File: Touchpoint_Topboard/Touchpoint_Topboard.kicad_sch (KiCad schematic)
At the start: 0 parts

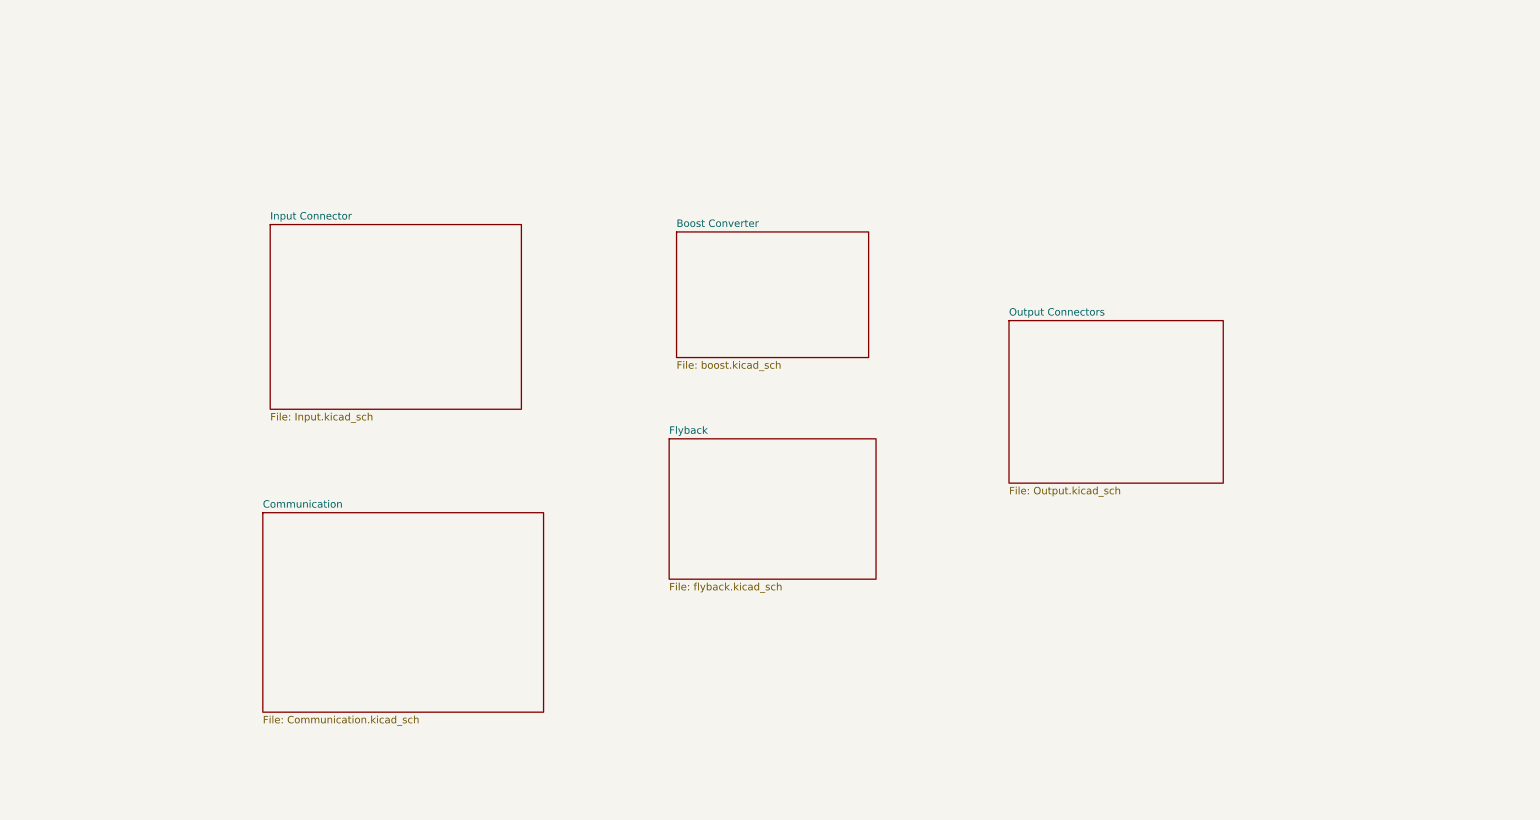
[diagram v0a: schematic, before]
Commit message: Added remaining interface things to topboard schematic
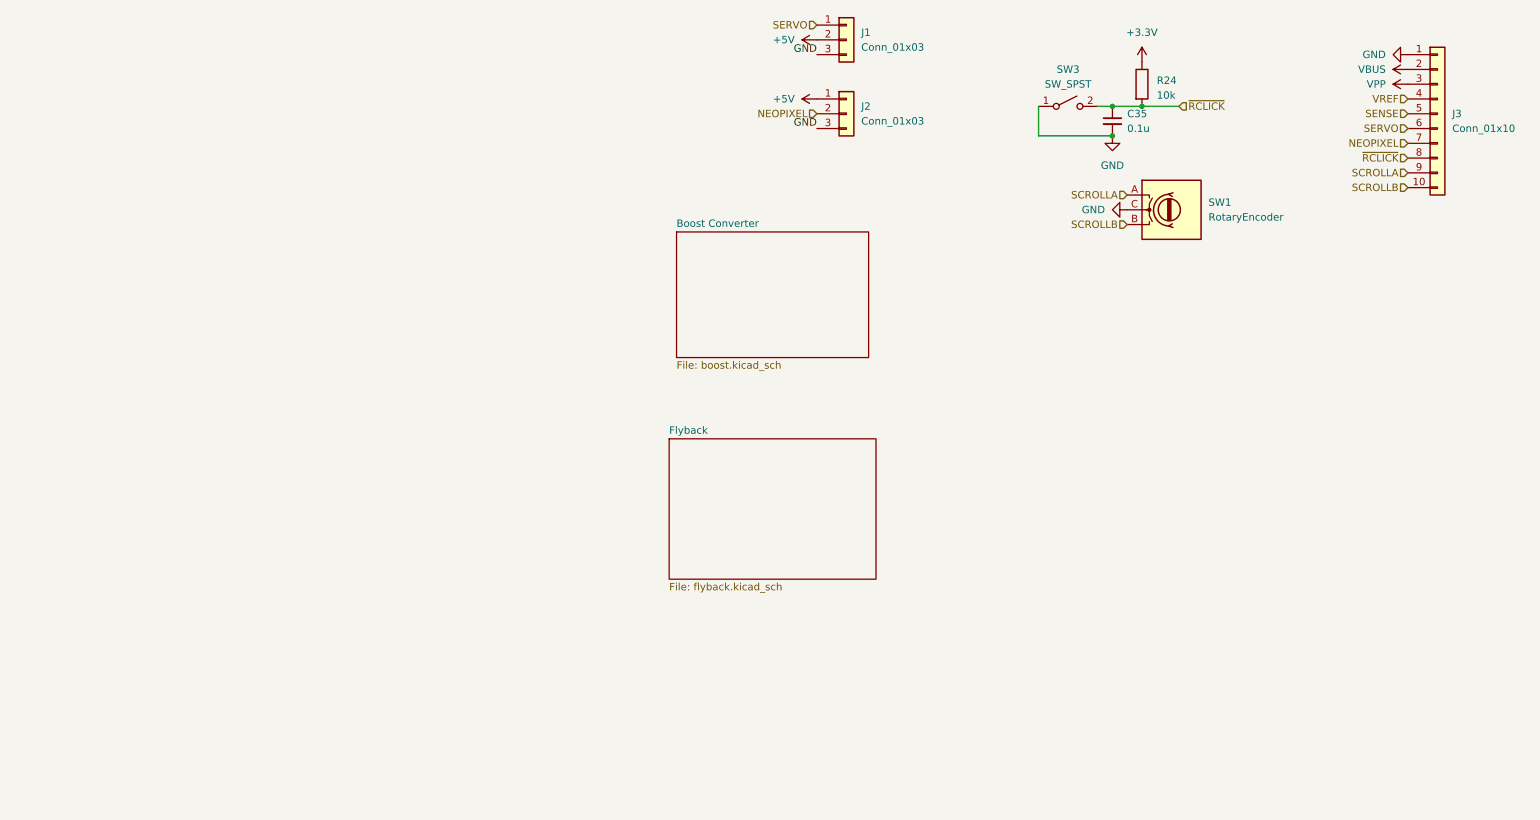
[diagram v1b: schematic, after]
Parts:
- added C35: 0.1u, Capacitor_SMD:C_0402_1005Metric, symbol Device:C_Small
- added J1, J2: Conn_01x03, symbol Connector_Generic:Conn_01x03
- added J3: Conn_01x10, symbol Connector_Generic:Conn_01x10
- added R24: 10k, Resistor_SMD:R_0402_1005Metric, symbol Device:R
- added SW1: RotaryEncoder, symbol Device:RotaryEncoder
- added SW3: SW_SPST, Button_Switch_THT:SW_PUSH_6mm, symbol Switch:SW_SPST
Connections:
- new net +3.3V: R24.1
- new net +5V: J1.2 (Pin_2), J2.1 (Pin_1)
- new net GND: C35.2, J1.3 (Pin_3), J2.3 (Pin_3), J3.1 (Pin_1), SW1.C, SW3.1 (A)
- new net NEOPIXEL: J2.2 (Pin_2), J3.7 (Pin_7)
- new net SCROLLA: J3.9 (Pin_9), SW1.A
- new net SCROLLB: J3.10 (Pin_10), SW1.B
- new net SENSE: J3.5 (Pin_5)
- new net SERVO: J1.1 (Pin_1), J3.6 (Pin_6)
- new net VBUS: J3.2 (Pin_2)
- new net VPP: J3.3 (Pin_3)
- new net VREF: J3.4 (Pin_4)
- new net ~{RCLICK}: C35.1, J3.8 (Pin_8), R24.2, SW3.2 (B)
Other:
- removed sheet Communication
- removed sheet Input Connector
- removed sheet Output Connectors

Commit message: Finished assigning most footprints
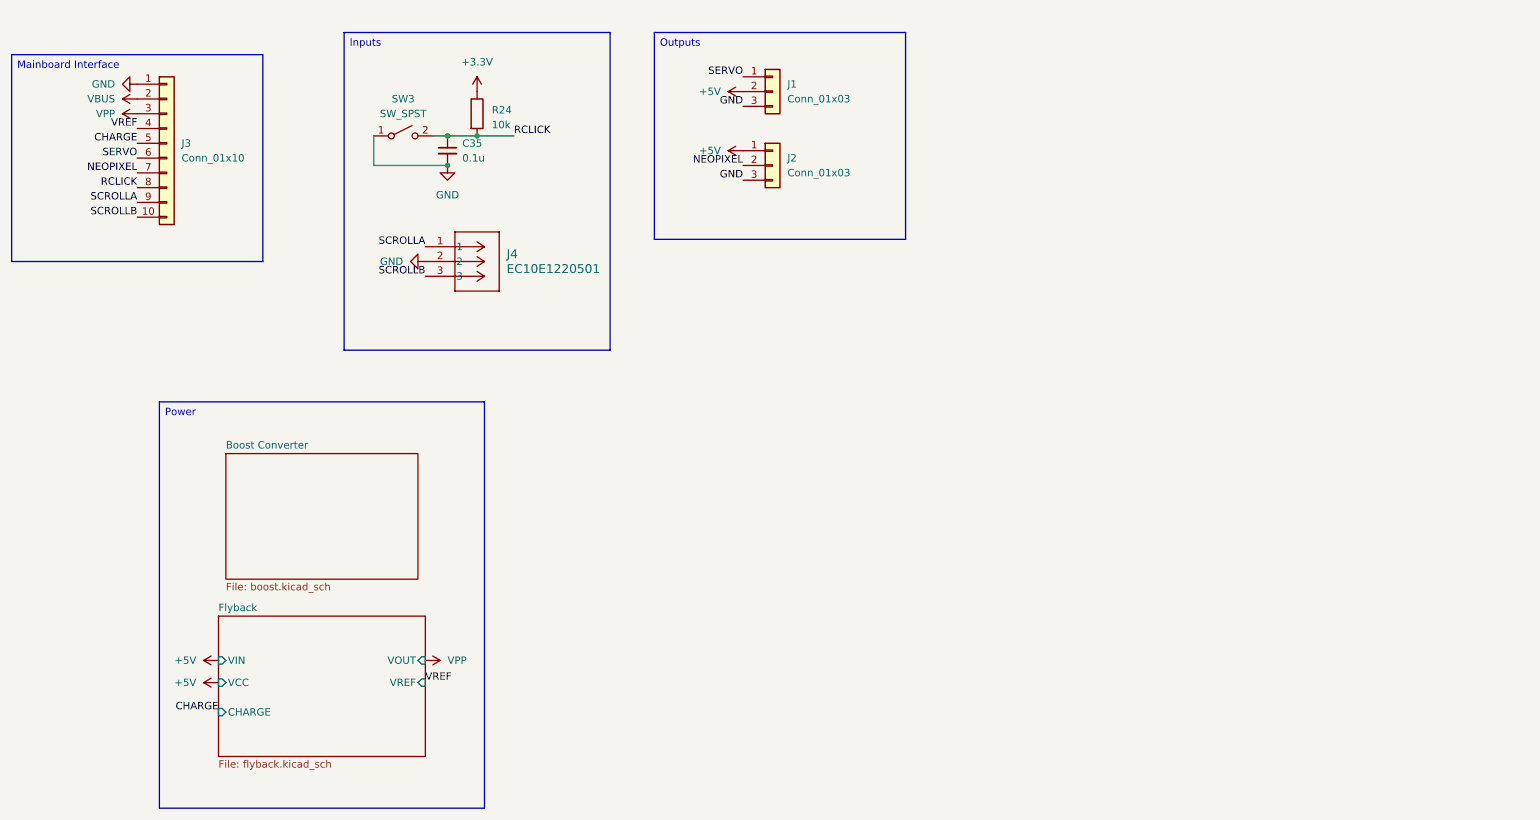
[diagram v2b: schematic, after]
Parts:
- removed SW1: RotaryEncoder, symbol Device:RotaryEncoder
- added J4: EC10E1220501, Touchpoint:CONN03_EC10E_9P8X6P1_ALPS, symbol EC10E122:EC10E1220501
- J1, J2: footprint (none) -> Connector_PinHeader_2.54mm:PinHeader_1x03_P2.54mm_Vertical
- J3: footprint (none) -> Connector_PinSocket_2.54mm:PinSocket_1x10_P2.54mm_Vertical
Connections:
- net GND: now also J4.2
- net SCROLLA: now also J4.1
- net SCROLLB: now also J4.3
- net SENSE renamed CHARGE
- net ~{RCLICK} renamed RCLICK
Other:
- sheet Flyback ports: added CHARGE, VCC, VIN, VOUT, VREF; removed none
- moved on the sheet: C35, J1, J2, J3, R24, SW3

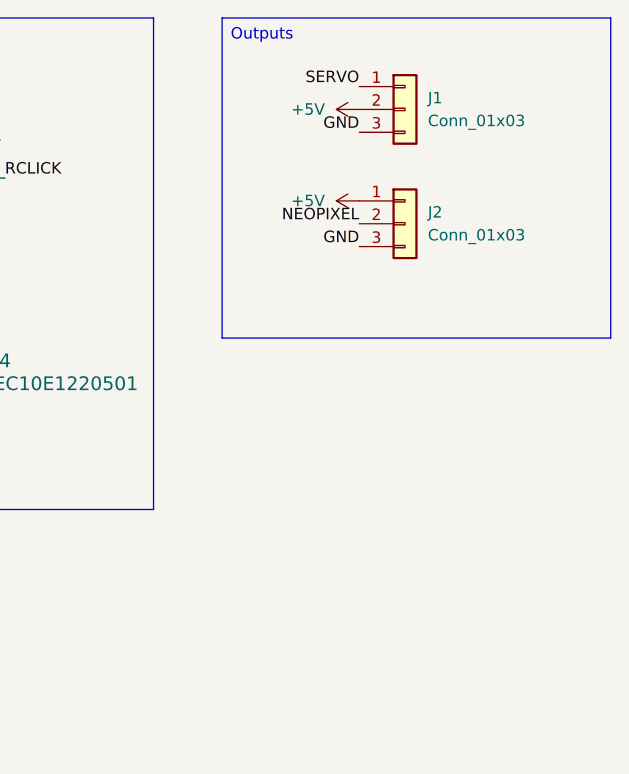
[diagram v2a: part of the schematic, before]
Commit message: Changed some component values based on availability
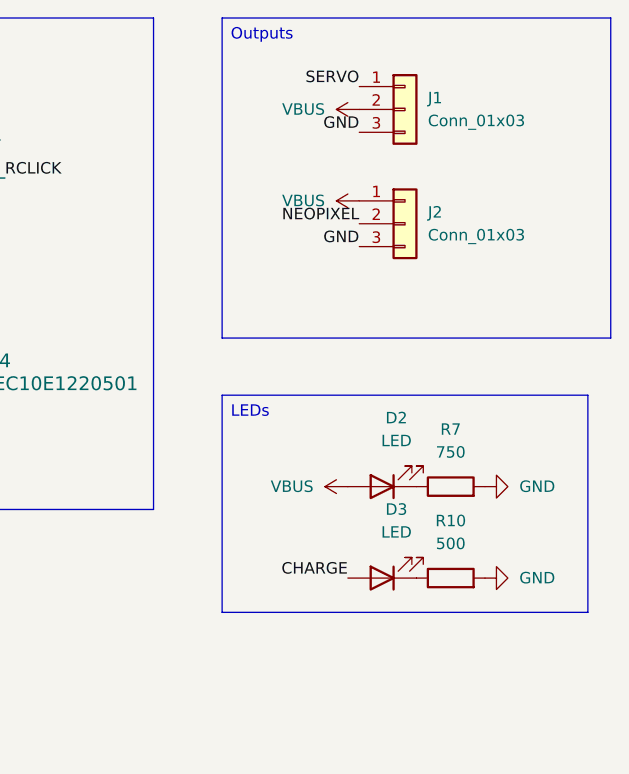
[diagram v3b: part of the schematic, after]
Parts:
- added D2, D3: LED, LED_SMD:LED_0603_1608Metric, symbol Device:LED
- added R10: 500, Resistor_SMD:R_0402_1005Metric, symbol Device:R
- added R7: 750, Resistor_SMD:R_0402_1005Metric, symbol Device:R
- SW3: footprint Button_Switch_THT:SW_PUSH_6mm -> (none)
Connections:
- net +5V: no longer J1.2 (Pin_2), J2.1 (Pin_1)
- net CHARGE: now also D3.2 (A)
- net GND: now also R10.2, R7.2
- net VBUS: now also J1.2 (Pin_2), J2.1 (Pin_1), D2.2 (A)
- new net: D2.1 (K), R7.1
- new net: D3.1 (K), R10.1

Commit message: Finished assigning footprints and 3d models for both boards
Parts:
- SW3: footprint (none) -> Touchpoint:SW_SPST_EVQP0
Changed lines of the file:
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@@
 			)
 		)
-		(property "Footprint" ""
+		(property "Footprint" "Touchpoint:SW_SPST_EVQP0"
 			(at 86.36 36.83 0)
 			(effects

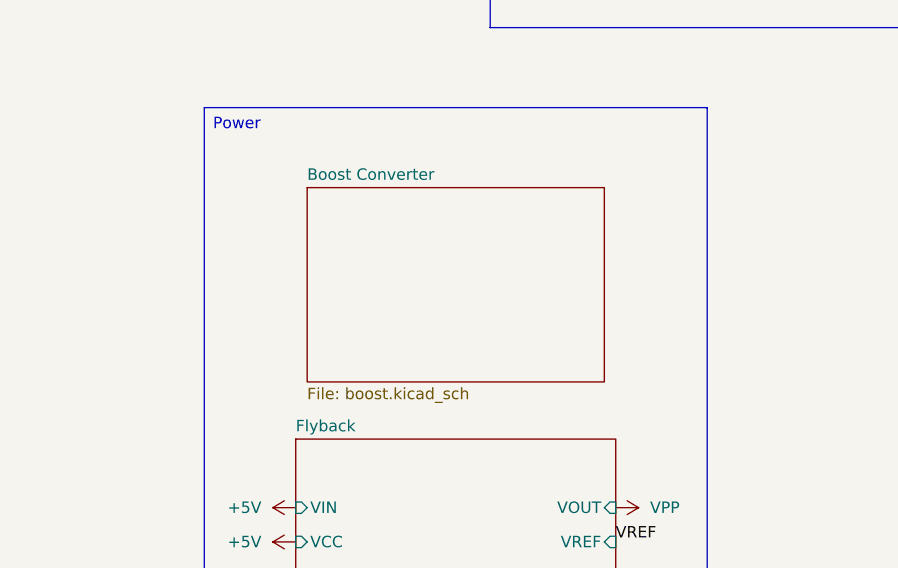
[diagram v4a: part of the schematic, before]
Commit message: Added 5V regulator to flyback converter
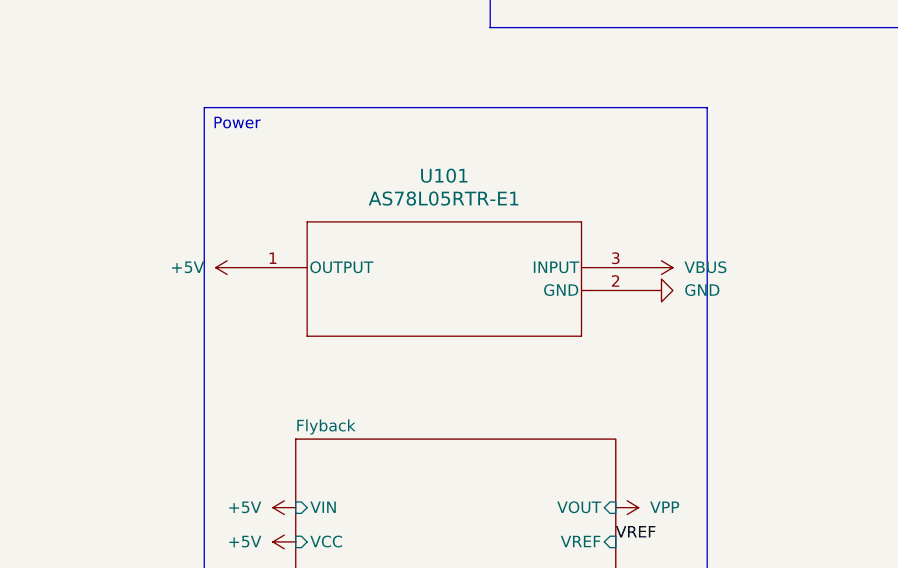
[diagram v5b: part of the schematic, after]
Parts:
- added U101: AS78L05RTR-E1, Touchpoint:SOT-89_3MC_MCH, symbol AS78LO5RTR:AS78L05RTR-E1
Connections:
- net +5V: now also U101.1 (OUTPUT)
- net GND: now also U101.2 (GND)
- net VBUS: now also U101.3 (INPUT)
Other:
- removed sheet Boost Converter

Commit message: Changed to jumper connector between boards
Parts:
- J3: footprint Connector_PinSocket_2.54mm:PinSocket_1x10_P2.54mm_Vertical -> Touchpoint:Jumper_Interface_10
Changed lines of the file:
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@@
 			)
 		)
-		(property "Footprint" "Connector_PinSocket_2.54mm:PinSocket_1x10_P2.54mm_Vertical"
+		(property "Footprint" "Touchpoint:Jumper_Interface_10"
 			(at 45.72 38.1 0)
 			(effects

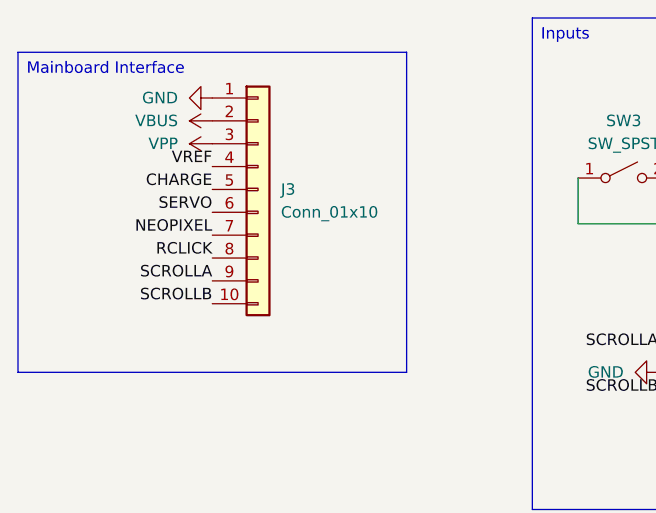
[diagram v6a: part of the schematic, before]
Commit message: Finished Routing and Placement of Top Board
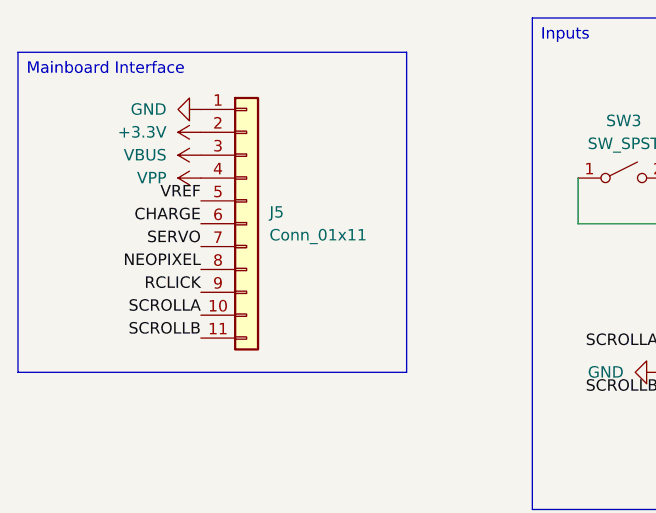
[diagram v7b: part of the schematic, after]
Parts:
- removed J3: Conn_01x10, Touchpoint:Jumper_Interface_10, symbol Connector_Generic:Conn_01x10
- added J5: Conn_01x11, symbol Connector_Generic:Conn_01x11
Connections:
- net +3.3V: now also J5.2 (Pin_2)
- net CHARGE: now also J5.6 (Pin_6)
- net GND: now also J5.1 (Pin_1)
- net NEOPIXEL: now also J5.8 (Pin_8)
- net RCLICK: now also J5.9 (Pin_9)
- net SCROLLA: now also J5.10 (Pin_10)
- net SCROLLB: now also J5.11 (Pin_11)
- net SERVO: now also J5.7 (Pin_7)
- net VBUS: now also J5.3 (Pin_3)
- net VPP: now also J5.4 (Pin_4)
- net VREF: now also J5.5 (Pin_5)
